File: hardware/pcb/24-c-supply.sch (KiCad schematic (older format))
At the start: 6 parts, among them U501 AMS1117-5.0, U502 AMS1117-3.3

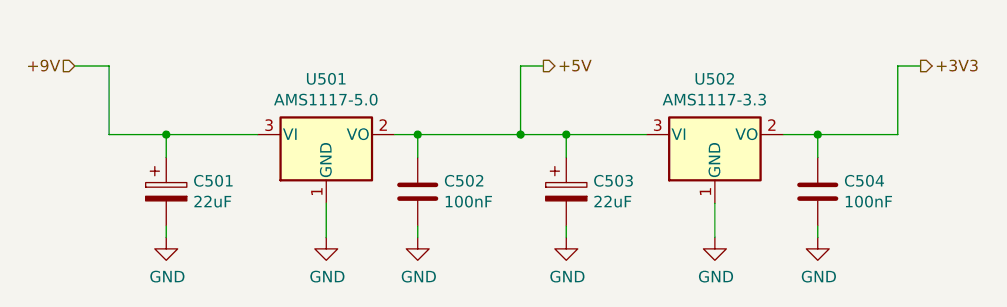
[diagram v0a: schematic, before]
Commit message: Footprints (#2)
* Changed uC

* Updated processor pins and added testpoints

* Small changes

* Updated footprints

* changed crystals

* Created footprints and archived project

* Added motor footprint, made init pcb
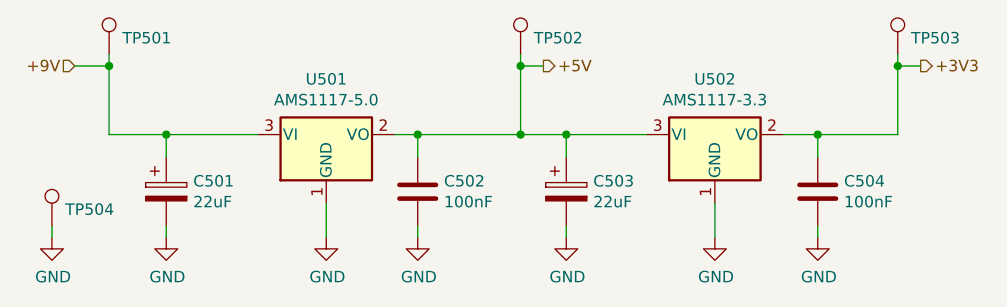
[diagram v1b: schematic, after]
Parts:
- added TP501: +9V, TestPoint:TestPoint_Pad_D2.0mm, symbol Connector:TestPoint
- added TP502: +5V, TestPoint:TestPoint_Pad_D2.0mm, symbol Connector:TestPoint
- added TP503: +3V3, TestPoint:TestPoint_Pad_D2.0mm, symbol Connector:TestPoint
- added TP504: GND, TestPoint:TestPoint_Pad_D2.0mm, symbol Connector:TestPoint
- C501, C503: footprint (none) -> Capacitor_SMD:C_Elec_10x10.2
- C502, C504: footprint C0603 -> Capacitor_SMD:C_0603_1608Metric
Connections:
- net +3V3: now also TP503.1
- net +5V: now also TP502.1
- net +9V: now also TP501.1
- net GND: now also TP504.1
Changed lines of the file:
@@
 F 0 "C502" H 5915 3446 50  0000 L CNN
 F 1 "100nF" H 5915 3355 50  0000 L CNN
-F 2 "C0603" H 5838 3250 50  0001 C CNN
+F 2 "Capacitor_SMD:C_0603_1608Metric" H 5838 3250 50  0001 C CNN
 F 3 "~" H 5800 3400 50  0001 C CNN
 	1    5800 3400
@@
 F 0 "C504" H 7665 3446 50  0000 L CNN
 F 1 "100nF" H 7665 3355 50  0000 L CNN
-F 2 "C0603" H 7588 3250 50  0001 C CNN
+F 2 "Capacitor_SMD:C_0603_1608Metric" H 7588 3250 50  0001 C CNN
 F 3 "~" H 7550 3400 50  0001 C CNN
 	1    7550 3400
@@
 F 0 "C501" H 4818 3446 50  0000 L CNN
 F 1 "22uF" H 4818 3355 50  0000 L CNN
-F 2 "" H 4738 3250 50  0001 C CNN
+F 2 "Capacitor_SMD:C_Elec_10x10.2" H 4738 3250 50  0001 C CNN
 F 3 "~" H 4700 3400 50  0001 C CNN
 	1    4700 3400
@@
 F 0 "C503" H 6568 3446 50  0000 L CNN
 F 1 "22uF" H 6568 3355 50  0000 L CNN
-F 2 "" H 6488 3250 50  0001 C CNN
+F 2 "Capacitor_SMD:C_Elec_10x10.2" H 6488 3250 50  0001 C CNN
 F 3 "~" H 6450 3400 50  0001 C CNN
 	1    6450 3400
@@
 Wire Wire Line
 	4450 2850 4300 2850
+$Comp
+L Connector:TestPoint TP501
+U 1 1 5FF9221C
+P 4450 2800
+F 0 "TP501" H 4508 2872 50  0000 L CNN
+F 1 "+9V" H 4508 2827 50  0001 L CNN
+F 2 "TestPoint:TestPoint_Pad_D2.0mm" H 4650 2800 50  0001 C CNN
+F 3 "~" H 4650 2800 50  0001 C CNN
+	1    4450 2800
+	1    0    0    -1
+$EndComp
+$Comp
+L Connector:TestPoint TP502
+U 1 1 5FF928DB
+P 6250 2800
+F 0 "TP502" H 6308 2872 50  0000 L CNN
+F 1 "+5V" H 6308 2827 50  0001 L CNN
+F 2 "TestPoint:TestPoint_Pad_D2.0mm" H 6450 2800 50  0001 C CNN
+F 3 "~" H 6450 2800 50  0001 C CNN
+	1    6250 2800
+	1    0    0    -1
+$EndComp
+$Comp
+L Connector:TestPoint TP503
+U 1 1 5FF92AF1
+P 7900 2800
+F 0 "TP503" H 7958 2872 50  0000 L CNN
+F 1 "+3V3" H 7958 2827 50  0001 L CNN
+F 2 "TestPoint:TestPoint_Pad_D2.0mm" H 8100 2800 50  0001 C CNN
+F 3 "~" H 8100 2800 50  0001 C CNN
+	1    7900 2800
+	1    0    0    -1
+$EndComp
+$Comp
+L Connector:TestPoint TP504
+U 1 1 5FF92EFF
+P 4200 3550
+F 0 "TP504" H 4258 3622 50  0000 L CNN
+F 1 "GND" H 4258 3577 50  0001 L CNN
+F 2 "TestPoint:TestPoint_Pad_D2.0mm" H 4400 3550 50  0001 C CNN
+F 3 "~" H 4400 3550 50  0001 C CNN
+	1    4200 3550
+	1    0    0    -1
+$EndComp
+$Comp
+L power:GND #PWR0507
+U 1 1 5FF9385B
+P 4200 3600
+F 0 "#PWR0507" H 4200 3350 50  0001 C CNN
+F 1 "GND" H 4205 3427 50  0000 C CNN
+F 2 "" H 4200 3600 50  0001 C CNN
+F 3 "" H 4200 3600 50  0001 C CNN
+	1    4200 3600
+	1    0    0    -1
+$EndComp
+Wire Wire Line
+	4200 3600 4200 3550
+Wire Wire Line
+	4450 2800 4450 2850
+Connection ~ 4450 2850
+Wire Wire Line
+	6250 2800 6250 2850
+Connection ~ 6250 2850
+Wire Wire Line
+	7900 2800 7900 2850
+Connection ~ 7900 2850
 $EndSCHEMATC

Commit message: Finished PCB (#3)
* Created PCB outline and first placement

* Changed connectors

* Minor

* Included all 3D files

* Mixed changes

* Changed supply to 7V

* Archived PCB project

* Update 24-clocks-rescue.lib

* First placement

* Routed supplies

* Update 24-clocks.kicad_pcb

* Added routing

* Routed more nets

* Finished routing

* Archived project

* Replace hash and date

* minor

* Update pcb.yml

* Update pcb.yml

* Update pcb.yml

* Update pcb.yml

* Auto update commit date and hash

* Update output

* changed outputs

* Added layer to output

* Update hash and date also in sch

* Added caps to hall sensors

* Cleanup files
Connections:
- net +9V renamed +7V
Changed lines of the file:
@@
 EESchema Schematic File Version 4
-LIBS:24-clocks-cache
-EELAYER 29 0
+EELAYER 30 0
 EELAYER END
 $Descr A4 11693 8268
@@
 Sheet 5 7
 Title "24 Clocks"
-Date "2020-12-06"
-Rev "V0.x"
+Date "GITDATE"
+Rev "GITHASH"
 Comp "Martin van Leussen"
 Comment1 ""
@@
 	4450 3150 4700 3150
 Text HLabel 4300 2850 0    50   Input ~ 0
-+9V
++7V
 Text HLabel 6350 2850 2    50   Output ~ 0
 +5V
